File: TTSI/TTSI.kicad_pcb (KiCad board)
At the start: 2 copper layers, 71 x 46 mm, 36 parts, among them Q101 Q_NMOS_GSD, Q102 Q_NMOS_GSD, Q103 Q_NMOS_GSD, Q104 Q_PMOS_GSD, Q105 Q_NMOS_GSD, Q106 Q_NMOS_GSD, U101 641964-1, U102 641964-1, U103 R-78E5.0-0.5, U104 74AHC1G32, U105 641964-1, U106 74AHC1G08, U107 LM555xM

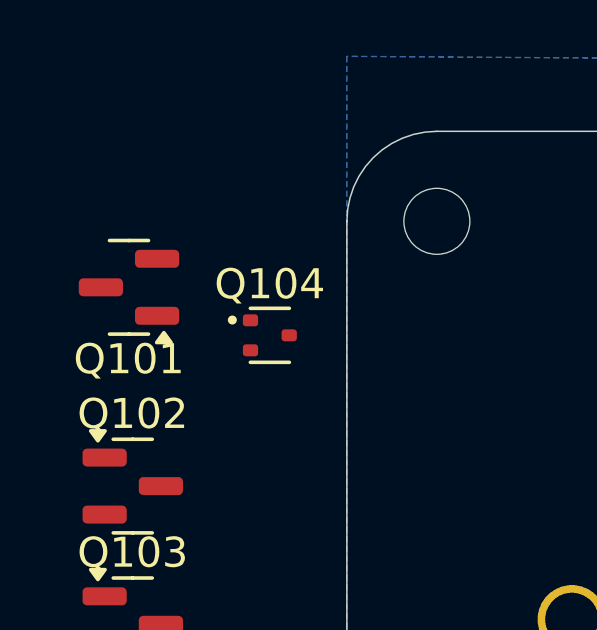
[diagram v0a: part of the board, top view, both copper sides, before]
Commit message: Fixes to BSPD
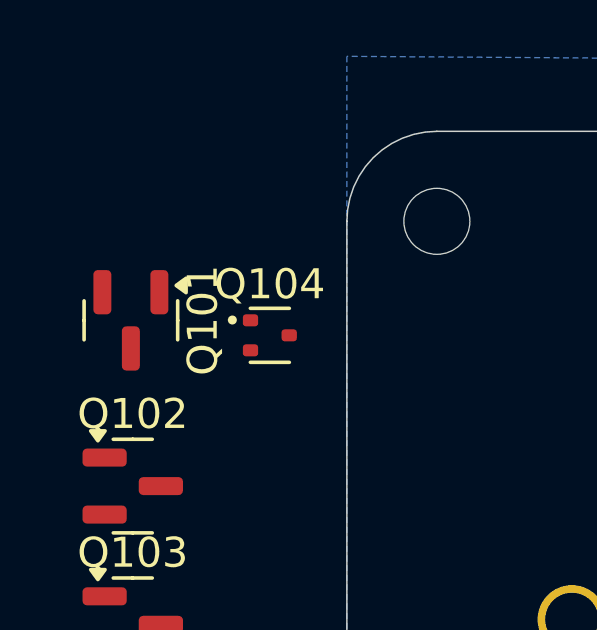
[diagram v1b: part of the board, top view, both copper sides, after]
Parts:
- moved Q101 1.10 mm to (114.8, 88.3), turned to -90 degrees
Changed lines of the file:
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@@
 	(footprint "Package_TO_SOT_SMD:SOT-23"
 		(layer "F.Cu")
-		(at 114.7375 87.2 180)
+		(at 114.8 88.3 -90)
 		(descr "SOT, 3 Pin (JEDEC TO-236 Var AB https://www.jedec.org/document_search?search_api_views_fulltext=TO-236), generated with kicad-footprint-generator ipc_gullwing_generator.py")
 		(tags "SOT TO_SOT_SMD")
 		(property "Reference" "Q101"
-			(at 0 -2.4 0)
+			(at 0 -2.4 90)
 			(layer "F.SilkS")
 			(effects
@@
 		)
 		(property "Value" "Q_NMOS_GSD"
-			(at 0 2.4 0)
+			(at 0 2.4 90)
 			(layer "F.Fab")
 			(effects
@@
 		)
 		(property "Datasheet" ""
-			(at 0 0 0)
+			(at 0 0 90)
 			(layer "F.Fab")
 			(hide yes)
@@
 		)
 		(property "Description" "N-MOSFET transistor, gate/source/drain"
-			(at 0 0 0)
+			(at 0 0 90)
 			(layer "F.Fab")
 			(hide yes)
@@
 		)
 		(property "JLC#" " C151421"
-			(at 0 0 180)
+			(at 0 0 270)
 			(unlocked yes)
 			(layer "F.Fab")
@@
 		)
 		(property "Sim.Device" ""
-			(at 0 0 180)
+			(at 0 0 270)
 			(unlocked yes)
 			(layer "F.Fab")
@@
 		)
 		(property "Sim.Type" ""
-			(at 0 0 180)
+			(at 0 0 270)
 			(unlocked yes)
 			(layer "F.Fab")
@@
 		(fp_line
 			(start 0 1.56)
+			(end -0.65 1.56)
+			(stroke
+				(width 0.12)
+				(type solid)
+			)
+			(layer "F.SilkS")
+		)
+		(fp_line
+			(start 0 1.56)
 			(end 0.65 1.56)
 			(stroke
@@
 		)
 		(fp_line
-			(start 0 1.56)
-			(end -0.65 1.56)
+			(start 0 -1.56)
+			(end -0.65 -1.56)
 			(stroke
 				(width 0.12)
@@
 			(start 0 -1.56)
 			(end 0.65 -1.56)
-			(stroke
-				(width 0.12)
-				(type solid)
-			)
-			(layer "F.SilkS")
-		)
-		(fp_line
-			(start 0 -1.56)
-			(end -0.65 -1.56)
 			(stroke
 				(width 0.12)
@@
 		)
 		(fp_line
+			(start -1.92 1.7)
+			(end 1.92 1.7)
+			(stroke
+				(width 0.05)
+				(type solid)
+			)
+			(layer "F.CrtYd")
+		)
+		(fp_line
 			(start 1.92 1.7)
 			(end 1.92 -1.7)
@@
 		)
 		(fp_line
+			(start -1.92 -1.7)
+			(end -1.92 1.7)
+			(stroke
+				(width 0.05)
+				(type solid)
+			)
+			(layer "F.CrtYd")
+		)
+		(fp_line
 			(start 1.92 -1.7)
 			(end -1.92 -1.7)
@@
 		)
 		(fp_line
-			(start -1.92 1.7)
-			(end 1.92 1.7)
-			(stroke
-				(width 0.05)
-				(type solid)
-			)
-			(layer "F.CrtYd")
-		)
-		(fp_line
-			(start -1.92 -1.7)
-			(end -1.92 1.7)
-			(stroke
-				(width 0.05)
-				(type solid)
-			)
-			(layer "F.CrtYd")
+			(start -0.65 1.45)
+			(end -0.65 -1.125)
+			(stroke
+				(width 0.1)
+				(type solid)
+			)
+			(layer "F.Fab")
 		)
 		(fp_line
@@
 		)
 		(fp_line
+			(start -0.65 -1.125)
+			(end -0.325 -1.45)
+			(stroke
+				(width 0.1)
+				(type solid)
+			)
+			(layer "F.Fab")
+		)
+		(fp_line
+			(start -0.325 -1.45)
+			(end 0.65 -1.45)
+			(stroke
+				(width 0.1)
+				(type solid)
+			)
+			(layer "F.Fab")
+		)
+		(fp_line
 			(start 0.65 -1.45)
 			(end 0.65 1.45)
@@
 			(layer "F.Fab")
 		)
-		(fp_line
-			(start -0.325 -1.45)
-			(end 0.65 -1.45)
-			(stroke
-				(width 0.1)
-				(type solid)
-			)
-			(layer "F.Fab")
-		)
-		(fp_line
-			(start -0.65 1.45)
-			(end -0.65 -1.125)
-			(stroke
-				(width 0.1)
-				(type solid)
-			)
-			(layer "F.Fab")
-		)
-		(fp_line
-			(start -0.65 -1.125)
-			(end -0.325 -1.45)
-			(stroke
-				(width 0.1)
-				(type solid)
-			)
-			(layer "F.Fab")
-		)
 		(fp_text user "${REFERENCE}"
-			(at 0 0 0)
+			(at 0 0 90)
 			(layer "F.Fab")
 			(effects
@@
 		)
 		(pad "1" smd roundrect
-			(at -0.9375 -0.95 180)
+			(at -0.9375 -0.95 270)
 			(size 1.475 0.6)
 			(layers "F.Cu" "F.Mask" "F.Paste")
@@
 		)
 		(pad "2" smd roundrect
-			(at -0.9375 0.95 180)
+			(at -0.9375 0.95 270)
 			(size 1.475 0.6)
 			(layers "F.Cu" "F.Mask" "F.Paste")
@@
 		)
 		(pad "3" smd roundrect
-			(at 0.9375 0 180)
+			(at 0.9375 0 270)
 			(size 1.475 0.6)
 			(layers "F.Cu" "F.Mask" "F.Paste")
